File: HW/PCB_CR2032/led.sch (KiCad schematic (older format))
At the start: 48 parts, among them M0 LED, M1 LED, M10 LED, M11 LED, M12 LED, M13 LED, M2 LED, M3 LED

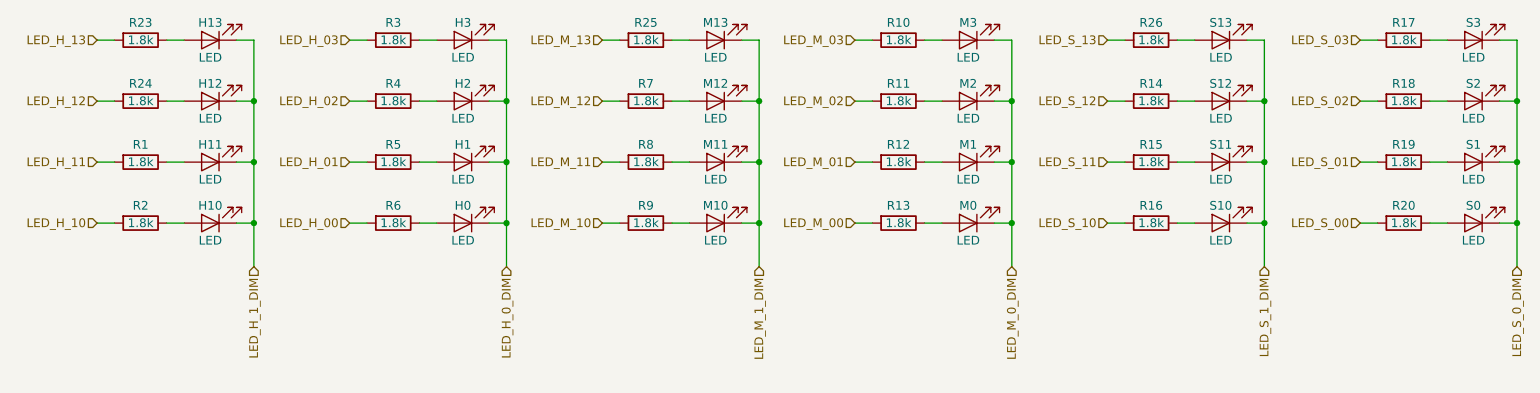
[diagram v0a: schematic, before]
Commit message: * Updated Schematic with 1206 leds and 1k 0805 current limiting resistors
* Restored STDC14 and debug UART, now shared with top led of minute and second. Some other LED pins remapped

* Updated STM32CubeMX project to reflect schematic changes and generated code again
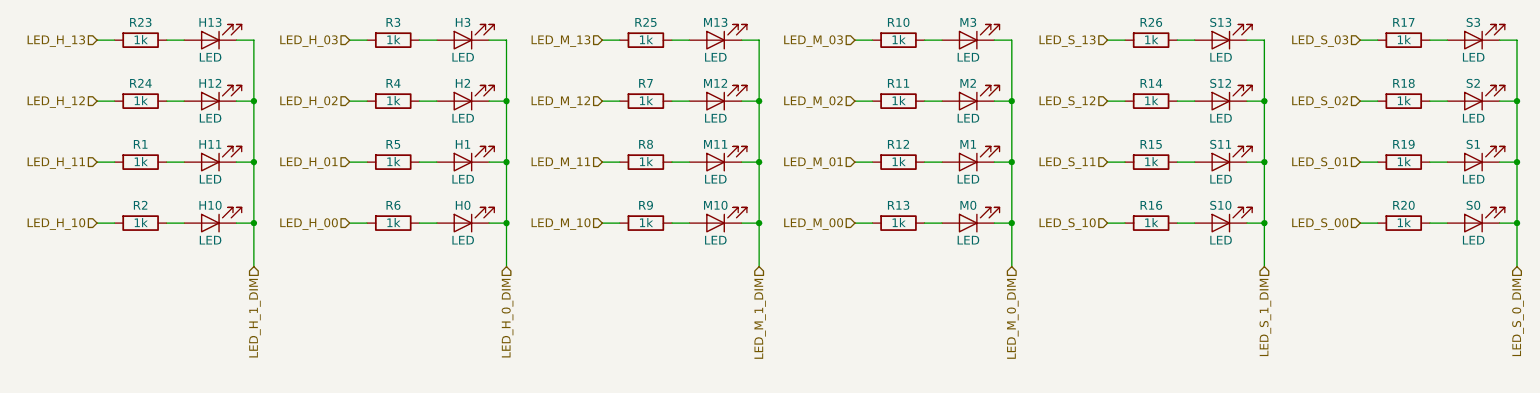
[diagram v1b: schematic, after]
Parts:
- H0, H1, H10, H11, H12, H13, H2, H3, M0, M1, M10, M11, M12, M13, M2, M3, S0, S1, S10, S11, S12, S13, S2, S3: footprint LED_SMD:LED_0603_1608Metric -> LED_SMD:LED_1206_3216Metric; Make (none) -> Kingbright; Mouser (none) -> 604-APTR3216SECKJ3; Part (none) -> APTR3216SECK/J3-PRV
- R1, R10, R11, R12, R13, R14, R15, R16, R17, R18, R19, R2, R20, R23, R24, R25, R26, R3, R4, R5, R6, R7, R8, R9: value 1.8k -> 1k; footprint Resistor_SMD:R_0603_1608Metric_Pad1.05x0.95mm_HandSolder -> Resistor_SMD:R_0805_2012Metric_Pad1.15x1.40mm_HandSolder; Make (none) -> Yageo; Mouser (none) -> 603-RC0805FR-071KL; Part (none) -> RC0805FR-071KL

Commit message: * Corrected LED references in schematic
* Corrected value of oscillator load capacitors

* Added HW readme with BoM
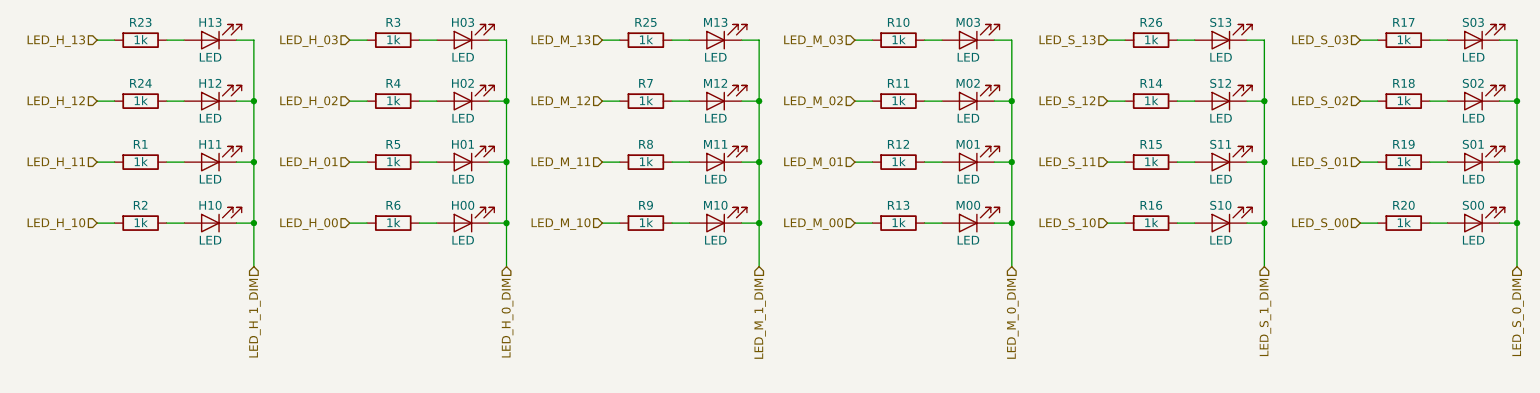
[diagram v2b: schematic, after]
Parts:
- renumbered H0 to H00, H1 to H01, H2 to H02, H3 to H03, M0 to M00, M1 to M01, M2 to M02, M3 to M03, S0 to S00, S1 to S01, S2 to S02, S3 to S03
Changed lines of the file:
@@
 	2550 3950 2650 3950
 $Comp
-L Device:LED H1
+L Device:LED H01
 U 1 1 5DC2A1A5
 P 4250 3600
-F 0 "H1" H 4250 3500 50  0000 C CNN
+F 0 "H01" H 4250 3500 50  0000 C CNN
 F 1 "LED" H 4250 3700 50  0000 C CNN
 F 2 "LED_SMD:LED_1206_3216Metric" H 4250 3600 50  0001 C CNN
@@
 $EndComp
 $Comp
-L Device:LED H0
+L Device:LED H00
 U 1 1 5DC2A1B9
 P 4250 3950
-F 0 "H0" H 4250 3850 50  0000 C CNN
+F 0 "H00" H 4250 3850 50  0000 C CNN
 F 1 "LED" H 4250 4050 50  0000 C CNN
 F 2 "LED_SMD:LED_1206_3216Metric" H 4250 3950 50  0001 C CNN
@@
 	4000 3950 4100 3950
 $Comp
-L Device:LED H3
+L Device:LED H03
 U 1 1 5DC38FA0
 P 4250 2900
-F 0 "H3" H 4250 2800 50  0000 C CNN
+F 0 "H03" H 4250 2800 50  0000 C CNN
 F 1 "LED" H 4250 3000 50  0000 C CNN
 F 2 "LED_SMD:LED_1206_3216Metric" H 4250 2900 50  0001 C CNN
@@
 $EndComp
 $Comp
-L Device:LED H2
+L Device:LED H02
 U 1 1 5DC38FB4
 P 4250 3250
-F 0 "H2" H 4250 3150 50  0000 C CNN
+F 0 "H02" H 4250 3150 50  0000 C CNN
 F 1 "LED" H 4250 3350 50  0000 C CNN
 F 2 "LED_SMD:LED_1206_3216Metric" H 4250 3250 50  0001 C CNN
@@
 	5450 3950 5550 3950
 $Comp
-L Device:LED M1
+L Device:LED M01
 U 1 1 5DC41E19
 P 7150 3600
-F 0 "M1" H 7150 3500 50  0000 C CNN
+F 0 "M01" H 7150 3500 50  0000 C CNN
 F 1 "LED" H 7150 3700 50  0000 C CNN
 F 2 "LED_SMD:LED_1206_3216Metric" H 7150 3600 50  0001 C CNN
@@
 $EndComp
 $Comp
-L Device:LED M0
+L Device:LED M00
 U 1 1 5DC41E2D
 P 7150 3950
-F 0 "M0" H 7150 3850 50  0000 C CNN
+F 0 "M00" H 7150 3850 50  0000 C CNN
 F 1 "LED" H 7150 4050 50  0000 C CNN
 F 2 "LED_SMD:LED_1206_3216Metric" H 7150 3950 50  0001 C CNN
@@
 	6900 3950 7000 3950
 $Comp
-L Device:LED M3
+L Device:LED M03
 U 1 1 5DC41E54
 P 7150 2900
-F 0 "M3" H 7150 2800 50  0000 C CNN
+F 0 "M03" H 7150 2800 50  0000 C CNN
 F 1 "LED" H 7150 3000 50  0000 C CNN
 F 2 "LED_SMD:LED_1206_3216Metric" H 7150 2900 50  0001 C CNN
@@
 $EndComp
 $Comp
-L Device:LED M2
+L Device:LED M02
 U 1 1 5DC41E68
 P 7150 3250
-F 0 "M2" H 7150 3150 50  0000 C CNN
+F 0 "M02" H 7150 3150 50  0000 C CNN
 F 1 "LED" H 7150 3350 50  0000 C CNN
 F 2 "LED_SMD:LED_1206_3216Metric" H 7150 3250 50  0001 C CNN
@@
 	8350 3950 8450 3950
 $Comp
-L Device:LED S1
+L Device:LED S01
 U 1 1 5DC5B83A
 P 10050 3600
-F 0 "S1" H 10050 3500 50  0000 C CNN
+F 0 "S01" H 10050 3500 50  0000 C CNN
 F 1 "LED" H 10050 3700 50  0000 C CNN
 F 2 "LED_SMD:LED_1206_3216Metric" H 10050 3600 50  0001 C CNN
@@
 $EndComp
 $Comp
-L Device:LED S0
+L Device:LED S00
 U 1 1 5DC5B84E
 P 10050 3950
-F 0 "S0" H 10050 3850 50  0000 C CNN
+F 0 "S00" H 10050 3850 50  0000 C CNN
 F 1 "LED" H 10050 4050 50  0000 C CNN
 F 2 "LED_SMD:LED_1206_3216Metric" H 10050 3950 50  0001 C CNN
@@
 	9800 3950 9900 3950
 $Comp
-L Device:LED S3
+L Device:LED S03
 U 1 1 5DC5B875
 P 10050 2900
-F 0 "S3" H 10050 2800 50  0000 C CNN
+F 0 "S03" H 10050 2800 50  0000 C CNN
 F 1 "LED" H 10050 3000 50  0000 C CNN
 F 2 "LED_SMD:LED_1206_3216Metric" H 10050 2900 50  0001 C CNN
@@
 $EndComp
 $Comp
-L Device:LED S2
+L Device:LED S02
 U 1 1 5DC5B889
 P 10050 3250
-F 0 "S2" H 10050 3150 50  0000 C CNN
+F 0 "S02" H 10050 3150 50  0000 C CNN
 F 1 "LED" H 10050 3350 50  0000 C CNN
 F 2 "LED_SMD:LED_1206_3216Metric" H 10050 3250 50  0001 C CNN

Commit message: Created layout for CR2032 version 1.0, for first prototype order, resulted in a lot of changes in the pin-mapping to make routing easier.
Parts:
- R1, R10, R11, R12, R13, R14, R15, R16, R17, R18, R19, R2, R20, R23, R24, R25, R26, R3, R4, R5, R6, R7, R8, R9: Make Yageo -> (none); Mouser 603-RC0805FR-071KL -> (none); Part RC0805FR-071KL -> (none)

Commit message: Worked on Rev 2.0 HW with smaller size.
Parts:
- R1, R10, R11, R12, R13, R14, R15, R16, R17, R18, R19, R2, R20, R23, R24, R25, R26, R3, R4, R5, R6, R7, R8, R9: footprint Resistor_SMD:R_0805_2012Metric_Pad1.15x1.40mm_HandSolder -> Resistor_SMD:R_0603_1608Metric_Pad1.05x0.95mm_HandSolder
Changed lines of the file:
@@
 F 0 "R1" V 2300 3600 50  0000 C CNN
 F 1 "1k" V 2400 3600 50  0000 C CNN
-F 2 "Resistor_SMD:R_0805_2012Metric_Pad1.15x1.40mm_HandSolder" V 2330 3600 50  0001 C CNN
+F 2 "Resistor_SMD:R_0603_1608Metric_Pad1.05x0.95mm_HandSolder" V 2330 3600 50  0001 C CNN
 F 3 "~" H 2400 3600 50  0001 C CNN
 F 4 "" H 2400 3600 50  0001 C CNN "Make"
@@
 F 0 "R2" V 2300 3950 50  0000 C CNN
 F 1 "1k" V 2400 3950 50  0000 C CNN
-F 2 "Resistor_SMD:R_0805_2012Metric_Pad1.15x1.40mm_HandSolder" V 2330 3950 50  0001 C CNN
+F 2 "Resistor_SMD:R_0603_1608Metric_Pad1.05x0.95mm_HandSolder" V 2330 3950 50  0001 C CNN
 F 3 "~" H 2400 3950 50  0001 C CNN
 F 4 "" H 2400 3950 50  0001 C CNN "Make"
@@
 F 0 "R5" V 3750 3600 50  0000 C CNN
 F 1 "1k" V 3850 3600 50  0000 C CNN
-F 2 "Resistor_SMD:R_0805_2012Metric_Pad1.15x1.40mm_HandSolder" V 3780 3600 50  0001 C CNN
+F 2 "Resistor_SMD:R_0603_1608Metric_Pad1.05x0.95mm_HandSolder" V 3780 3600 50  0001 C CNN
 F 3 "~" H 3850 3600 50  0001 C CNN
 F 4 "" H 3850 3600 50  0001 C CNN "Make"
@@
 F 0 "R6" V 3750 3950 50  0000 C CNN
 F 1 "1k" V 3850 3950 50  0000 C CNN
-F 2 "Resistor_SMD:R_0805_2012Metric_Pad1.15x1.40mm_HandSolder" V 3780 3950 50  0001 C CNN
+F 2 "Resistor_SMD:R_0603_1608Metric_Pad1.05x0.95mm_HandSolder" V 3780 3950 50  0001 C CNN
 F 3 "~" H 3850 3950 50  0001 C CNN
 F 4 "" H 3850 3950 50  0001 C CNN "Make"
@@
 F 0 "R3" V 3750 2900 50  0000 C CNN
 F 1 "1k" V 3850 2900 50  0000 C CNN
-F 2 "Resistor_SMD:R_0805_2012Metric_Pad1.15x1.40mm_HandSolder" V 3780 2900 50  0001 C CNN
+F 2 "Resistor_SMD:R_0603_1608Metric_Pad1.05x0.95mm_HandSolder" V 3780 2900 50  0001 C CNN
 F 3 "~" H 3850 2900 50  0001 C CNN
 F 4 "" H 3850 2900 50  0001 C CNN "Make"
@@
 F 0 "R4" V 3750 3250 50  0000 C CNN
 F 1 "1k" V 3850 3250 50  0000 C CNN
-F 2 "Resistor_SMD:R_0805_2012Metric_Pad1.15x1.40mm_HandSolder" V 3780 3250 50  0001 C CNN
+F 2 "Resistor_SMD:R_0603_1608Metric_Pad1.05x0.95mm_HandSolder" V 3780 3250 50  0001 C CNN
 F 3 "~" H 3850 3250 50  0001 C CNN
 F 4 "" H 3850 3250 50  0001 C CNN "Make"
@@
 F 0 "R8" V 5200 3600 50  0000 C CNN
 F 1 "1k" V 5300 3600 50  0000 C CNN
-F 2 "Resistor_SMD:R_0805_2012Metric_Pad1.15x1.40mm_HandSolder" V 5230 3600 50  0001 C CNN
+F 2 "Resistor_SMD:R_0603_1608Metric_Pad1.05x0.95mm_HandSolder" V 5230 3600 50  0001 C CNN
 F 3 "~" H 5300 3600 50  0001 C CNN
 F 4 "" H 5300 3600 50  0001 C CNN "Make"
@@
 F 0 "R9" V 5200 3950 50  0000 C CNN
 F 1 "1k" V 5300 3950 50  0000 C CNN
-F 2 "Resistor_SMD:R_0805_2012Metric_Pad1.15x1.40mm_HandSolder" V 5230 3950 50  0001 C CNN
+F 2 "Resistor_SMD:R_0603_1608Metric_Pad1.05x0.95mm_HandSolder" V 5230 3950 50  0001 C CNN
 F 3 "~" H 5300 3950 50  0001 C CNN
 F 4 "" H 5300 3950 50  0001 C CNN "Make"
@@
 F 0 "R12" V 6650 3600 50  0000 C CNN
 F 1 "1k" V 6750 3600 50  0000 C CNN
-F 2 "Resistor_SMD:R_0805_2012Metric_Pad1.15x1.40mm_HandSolder" V 6680 3600 50  0001 C CNN
+F 2 "Resistor_SMD:R_0603_1608Metric_Pad1.05x0.95mm_HandSolder" V 6680 3600 50  0001 C CNN
 F 3 "~" H 6750 3600 50  0001 C CNN
 F 4 "" H 6750 3600 50  0001 C CNN "Make"
@@
 F 0 "R13" V 6650 3950 50  0000 C CNN
 F 1 "1k" V 6750 3950 50  0000 C CNN
-F 2 "Resistor_SMD:R_0805_2012Metric_Pad1.15x1.40mm_HandSolder" V 6680 3950 50  0001 C CNN
+F 2 "Resistor_SMD:R_0603_1608Metric_Pad1.05x0.95mm_HandSolder" V 6680 3950 50  0001 C CNN
 F 3 "~" H 6750 3950 50  0001 C CNN
 F 4 "" H 6750 3950 50  0001 C CNN "Make"
@@
 F 0 "R10" V 6650 2900 50  0000 C CNN
 F 1 "1k" V 6750 2900 50  0000 C CNN
-F 2 "Resistor_SMD:R_0805_2012Metric_Pad1.15x1.40mm_HandSolder" V 6680 2900 50  0001 C CNN
+F 2 "Resistor_SMD:R_0603_1608Metric_Pad1.05x0.95mm_HandSolder" V 6680 2900 50  0001 C CNN
 F 3 "~" H 6750 2900 50  0001 C CNN
 F 4 "" H 6750 2900 50  0001 C CNN "Make"
@@
 F 0 "R11" V 6650 3250 50  0000 C CNN
 F 1 "1k" V 6750 3250 50  0000 C CNN
-F 2 "Resistor_SMD:R_0805_2012Metric_Pad1.15x1.40mm_HandSolder" V 6680 3250 50  0001 C CNN
+F 2 "Resistor_SMD:R_0603_1608Metric_Pad1.05x0.95mm_HandSolder" V 6680 3250 50  0001 C CNN
 F 3 "~" H 6750 3250 50  0001 C CNN
 F 4 "" H 6750 3250 50  0001 C CNN "Make"
@@
 F 0 "R7" V 5200 3250 50  0000 C CNN
 F 1 "1k" V 5300 3250 50  0000 C CNN
-F 2 "Resistor_SMD:R_0805_2012Metric_Pad1.15x1.40mm_HandSolder" V 5230 3250 50  0001 C CNN
+F 2 "Resistor_SMD:R_0603_1608Metric_Pad1.05x0.95mm_HandSolder" V 5230 3250 50  0001 C CNN
 F 3 "~" H 5300 3250 50  0001 C CNN
 F 4 "" H 5300 3250 50  0001 C CNN "Make"
@@
 F 0 "R15" V 8100 3600 50  0000 C CNN
 F 1 "1k" V 8200 3600 50  0000 C CNN
-F 2 "Resistor_SMD:R_0805_2012Metric_Pad1.15x1.40mm_HandSolder" V 8130 3600 50  0001 C CNN
+F 2 "Resistor_SMD:R_0603_1608Metric_Pad1.05x0.95mm_HandSolder" V 8130 3600 50  0001 C CNN
 F 3 "~" H 8200 3600 50  0001 C CNN
 F 4 "" H 8200 3600 50  0001 C CNN "Make"
@@
 F 0 "R16" V 8100 3950 50  0000 C CNN
 F 1 "1k" V 8200 3950 50  0000 C CNN
-F 2 "Resistor_SMD:R_0805_2012Metric_Pad1.15x1.40mm_HandSolder" V 8130 3950 50  0001 C CNN
+F 2 "Resistor_SMD:R_0603_1608Metric_Pad1.05x0.95mm_HandSolder" V 8130 3950 50  0001 C CNN
 F 3 "~" H 8200 3950 50  0001 C CNN
 F 4 "" H 8200 3950 50  0001 C CNN "Make"
@@
 F 0 "R19" V 9550 3600 50  0000 C CNN
 F 1 "1k" V 9650 3600 50  0000 C CNN
-F 2 "Resistor_SMD:R_0805_2012Metric_Pad1.15x1.40mm_HandSolder" V 9580 3600 50  0001 C CNN
+F 2 "Resistor_SMD:R_0603_1608Metric_Pad1.05x0.95mm_HandSolder" V 9580 3600 50  0001 C CNN
 F 3 "~" H 9650 3600 50  0001 C CNN
 F 4 "" H 9650 3600 50  0001 C CNN "Make"
@@
 F 0 "R20" V 9550 3950 50  0000 C CNN
 F 1 "1k" V 9650 3950 50  0000 C CNN
-F 2 "Resistor_SMD:R_0805_2012Metric_Pad1.15x1.40mm_HandSolder" V 9580 3950 50  0001 C CNN
+F 2 "Resistor_SMD:R_0603_1608Metric_Pad1.05x0.95mm_HandSolder" V 9580 3950 50  0001 C CNN
 F 3 "~" H 9650 3950 50  0001 C CNN
 F 4 "" H 9650 3950 50  0001 C CNN "Make"
@@
 F 0 "R17" V 9550 2900 50  0000 C CNN
 F 1 "1k" V 9650 2900 50  0000 C CNN
-F 2 "Resistor_SMD:R_0805_2012Metric_Pad1.15x1.40mm_HandSolder" V 9580 2900 50  0001 C CNN
+F 2 "Resistor_SMD:R_0603_1608Metric_Pad1.05x0.95mm_HandSolder" V 9580 2900 50  0001 C CNN
 F 3 "~" H 9650 2900 50  0001 C CNN
 F 4 "" H 9650 2900 50  0001 C CNN "Make"
@@
 F 0 "R18" V 9550 3250 50  0000 C CNN
 F 1 "1k" V 9650 3250 50  0000 C CNN
-F 2 "Resistor_SMD:R_0805_2012Metric_Pad1.15x1.40mm_HandSolder" V 9580 3250 50  0001 C CNN
+F 2 "Resistor_SMD:R_0603_1608Metric_Pad1.05x0.95mm_HandSolder" V 9580 3250 50  0001 C CNN
 F 3 "~" H 9650 3250 50  0001 C CNN
 F 4 "" H 9650 3250 50  0001 C CNN "Make"
@@
 F 0 "R14" V 8100 3250 50  0000 C CNN
 F 1 "1k" V 8200 3250 50  0000 C CNN
-F 2 "Resistor_SMD:R_0805_2012Metric_Pad1.15x1.40mm_HandSolder" V 8130 3250 50  0001 C CNN
+F 2 "Resistor_SMD:R_0603_1608Metric_Pad1.05x0.95mm_HandSolder" V 8130 3250 50  0001 C CNN
 F 3 "~" H 8200 3250 50  0001 C CNN
 F 4 "" H 8200 3250 50  0001 C CNN "Make"
@@
 F 0 "R24" V 2300 3250 50  0000 C CNN
 F 1 "1k" V 2400 3250 50  0000 C CNN
-F 2 "Resistor_SMD:R_0805_2012Metric_Pad1.15x1.40mm_HandSolder" V 2330 3250 50  0001 C CNN
+F 2 "Resistor_SMD:R_0603_1608Metric_Pad1.05x0.95mm_HandSolder" V 2330 3250 50  0001 C CNN
 F 3 "~" H 2400 3250 50  0001 C CNN
 F 4 "" H 2400 3250 50  0001 C CNN "Make"
@@
 F 0 "R23" V 2300 2900 50  0000 C CNN
 F 1 "1k" V 2400 2900 50  0000 C CNN
-F 2 "Resistor_SMD:R_0805_2012Metric_Pad1.15x1.40mm_HandSolder" V 2330 2900 50  0001 C CNN
+F 2 "Resistor_SMD:R_0603_1608Metric_Pad1.05x0.95mm_HandSolder" V 2330 2900 50  0001 C CNN
 F 3 "~" H 2400 2900 50  0001 C CNN
 F 4 "" H 2400 2900 50  0001 C CNN "Make"
@@
 F 0 "R25" V 5200 2900 50  0000 C CNN
 F 1 "1k" V 5300 2900 50  0000 C CNN
-F 2 "Resistor_SMD:R_0805_2012Metric_Pad1.15x1.40mm_HandSolder" V 5230 2900 50  0001 C CNN
+F 2 "Resistor_SMD:R_0603_1608Metric_Pad1.05x0.95mm_HandSolder" V 5230 2900 50  0001 C CNN
 F 3 "~" H 5300 2900 50  0001 C CNN
 F 4 "" H 5300 2900 50  0001 C CNN "Make"
@@
 F 0 "R26" V 8100 2900 50  0000 C CNN
 F 1 "1k" V 8200 2900 50  0000 C CNN
-F 2 "Resistor_SMD:R_0805_2012Metric_Pad1.15x1.40mm_HandSolder" V 8130 2900 50  0001 C CNN
+F 2 "Resistor_SMD:R_0603_1608Metric_Pad1.05x0.95mm_HandSolder" V 8130 2900 50  0001 C CNN
 F 3 "~" H 8200 2900 50  0001 C CNN
 F 4 "" H 8200 2900 50  0001 C CNN "Make"
